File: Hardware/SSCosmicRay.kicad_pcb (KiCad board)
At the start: 2 copper layers, 80 x 50 mm, 115 parts, among them J1 ICSP-PIC, J2 USB_MINI, J3 CONN-9, SW1 PGM, SW2 RST, U1 MAX4477, U2 MAX4477, U3 MAX991, U4 741G08, U5 PIC32MX250F128D, U6 MAX4477, U7 MAX4477, U8 LTC3129-SOP, U9 AOZ1280, X1 8MHz

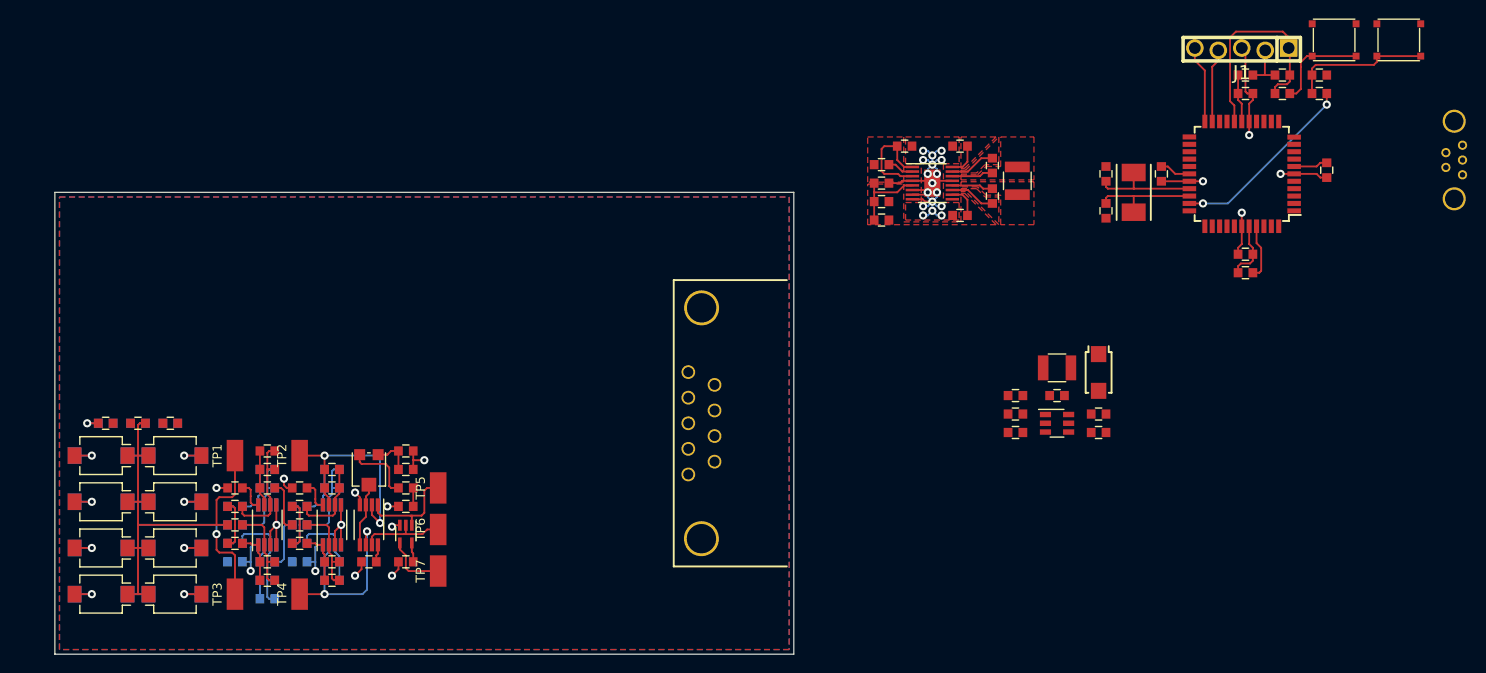
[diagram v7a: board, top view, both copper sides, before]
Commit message: Add additional photodiodes
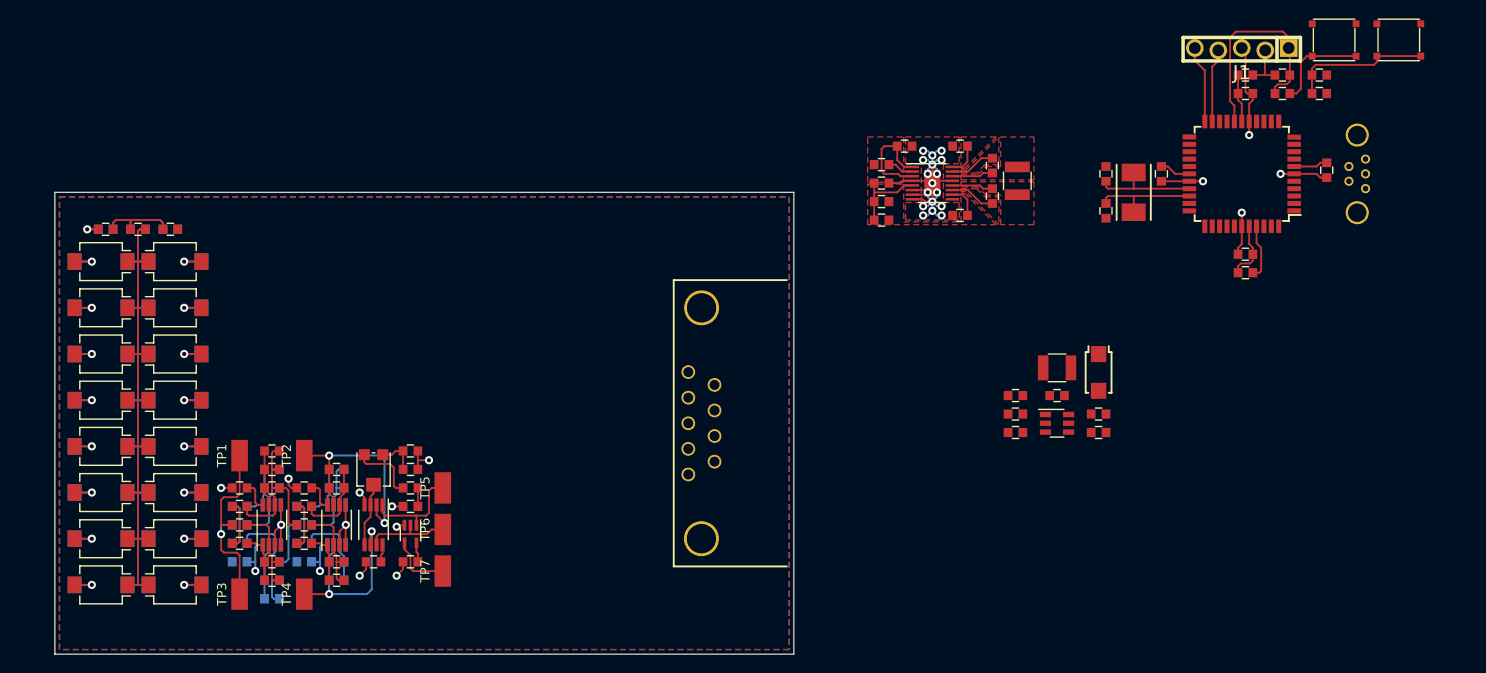
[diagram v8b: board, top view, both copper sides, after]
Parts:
- added D18: VBPW34FASR, DIOC-BPW34R, F.Cu at (132.0, 65.5)
- added D19: VBPW34FASR, DIOC-BPW34R, F.Cu at (140.0, 65.5)
- added D20: VBPW34FASR, DIOC-BPW34R, F.Cu at (132.0, 90.5)
- added D21: VBPW34FASR, DIOC-BPW34R, F.Cu at (140.0, 90.5)
- added D22: VBPW34FASR, DIOC-BPW34R, F.Cu at (132.0, 60.5)
- added D23: VBPW34FASR, DIOC-BPW34R, F.Cu at (140.0, 60.5)
- added D24: VBPW34FASR, DIOC-BPW34R, F.Cu at (132.0, 95.5)
- added D25: VBPW34FASR, DIOC-BPW34R, F.Cu at (140.0, 95.5)
- added D26: VBPW34FASR, DIOC-BPW34R, B.Cu at (132.0, 65.5)
- added D27: VBPW34FASR, DIOC-BPW34R, B.Cu at (140.0, 65.5)
- added D28: VBPW34FASR, DIOC-BPW34R, B.Cu at (132.0, 90.5)
- added D29: VBPW34FASR, DIOC-BPW34R, B.Cu at (140.0, 90.5)
- added D30: VBPW34FASR, DIOC-BPW34R, B.Cu at (132.0, 60.5)
- added D31: VBPW34FASR, DIOC-BPW34R, B.Cu at (140.0, 60.5)
- added D32: VBPW34FASR, DIOC-BPW34R, B.Cu at (132.0, 95.5)
- added D33: VBPW34FASR, DIOC-BPW34R, B.Cu at (140.0, 95.5)
- moved C1 21.0 mm to (132.5, 57.0)
- moved C31 21.0 mm to (132.5, 57.0)
- moved R1 21.0 mm to (139.5, 57.0)
- moved R2 21.0 mm to (136.0, 57.0)
- moved R23 21.0 mm to (139.5, 57.0)
- moved R24 21.0 mm to (136.0, 57.0)
- moved D1 11.0 mm to (132.0, 85.5)
- moved D10 11.0 mm to (140.0, 85.5)
- moved D11 11.0 mm to (132.0, 80.5)
- moved D12 11.0 mm to (140.0, 80.5)
- moved D13 11.0 mm to (132.0, 75.5)
- moved D14 11.0 mm to (140.0, 75.5)
- moved D15 11.0 mm to (132.0, 70.5)
- moved D16 11.0 mm to (140.0, 70.5)
- moved D2 11.0 mm to (140.0, 85.5)
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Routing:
- net GND: track 123.4 -> 153.3 mm, vias 40 -> 48
- net /Amplifier 2/In: track 47.1 -> 67.7 mm
- net /Amplifier 1/In: track 47.1 -> 67.7 mm
- net /Processor/PGM: track 20.5 -> 0.00 mm, vias 2 -> 0
- net N-000009: track 0.00 -> 8.05 mm
- net N-0000075: track 0.00 -> 8.05 mm
